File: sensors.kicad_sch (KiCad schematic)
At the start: 0 parts

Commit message: 1.2.7 Schematic design sheet #3: Sensors
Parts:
- added MK1: CMC-5042PF-AC, CMC-5042PF-AC:CUI_CMC-5042PF-AC, symbol CMC-5042PF-AC:CMC-5042PF-AC
- added Q1: TEMT6000X01, TEMT6000X01:TRANS_TEMT6000X01, symbol TEMT6000X01:TEMT6000X01
- added U2: BME280, BME280:PSON65P250X250X100-8N, symbol BME280:BME280
- added U7: MAX4466EXK, MAX4466EXK:SOT65P210X110-5N, symbol MAX4466EXK:MAX4466EXK
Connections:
- new net GND: U2.1 (GND), U2.7 (GND)

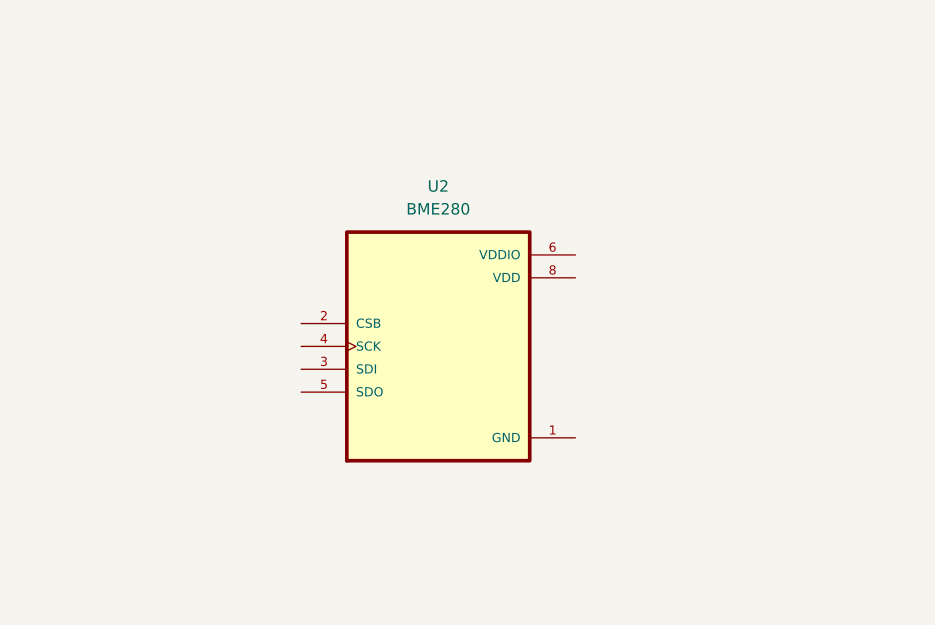
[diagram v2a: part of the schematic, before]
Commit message: 1.2.8 Design the BME280 subcircuit
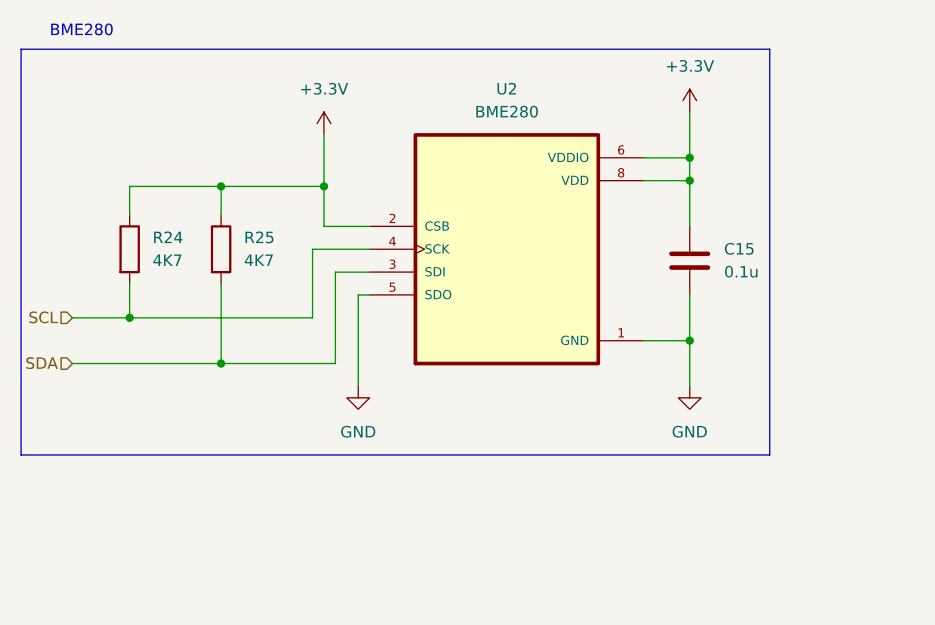
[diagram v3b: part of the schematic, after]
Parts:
- added C15: 0.1u, symbol Device:C
- added R24, R25: 4K7, symbol Device:R
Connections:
- net GND: now also U2.5 (SDO), C15.2
- net +3.3V: now reaches U2.2 (CSB)
- net +3.3V: now also U2.6 (VDDIO), U2.8 (VDD), C15.1, R24.1, R25.1
- net SDA: now reaches U2.3 (SDI)
- net SDA: now also R25.2
- net SCL: now reaches U2.4 (SCK)
- net SCL: now also R24.2
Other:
- note added: "BME280"
- moved on the sheet: U2

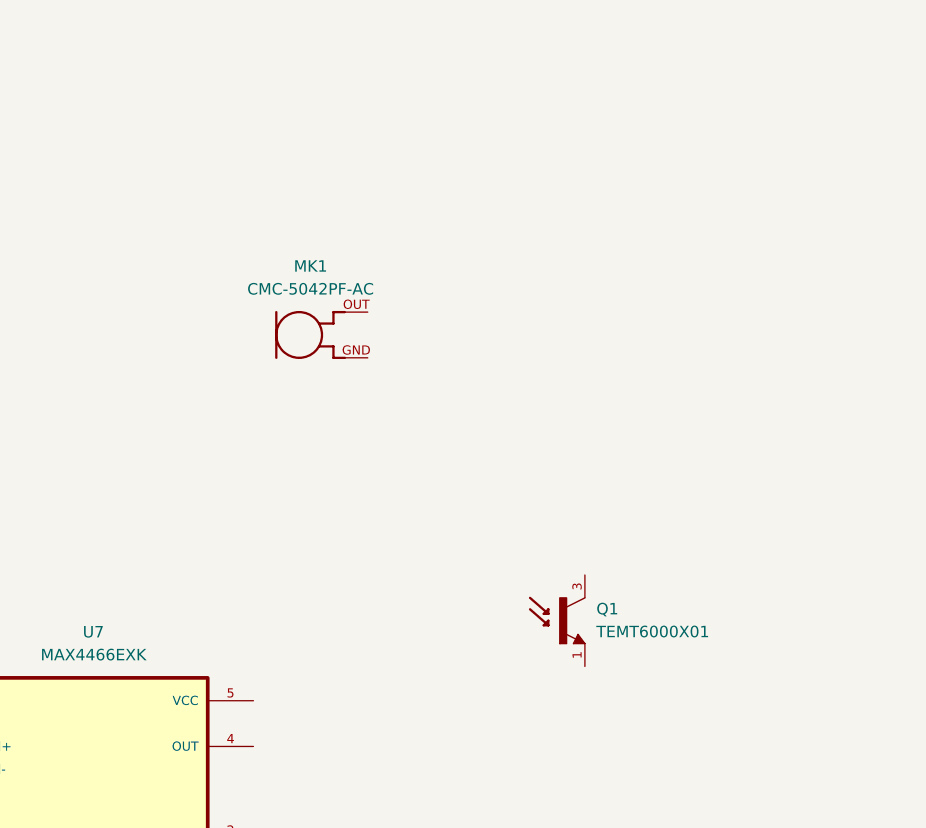
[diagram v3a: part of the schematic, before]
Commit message: 1.2.9 Design the ambient light sensor subcircuit
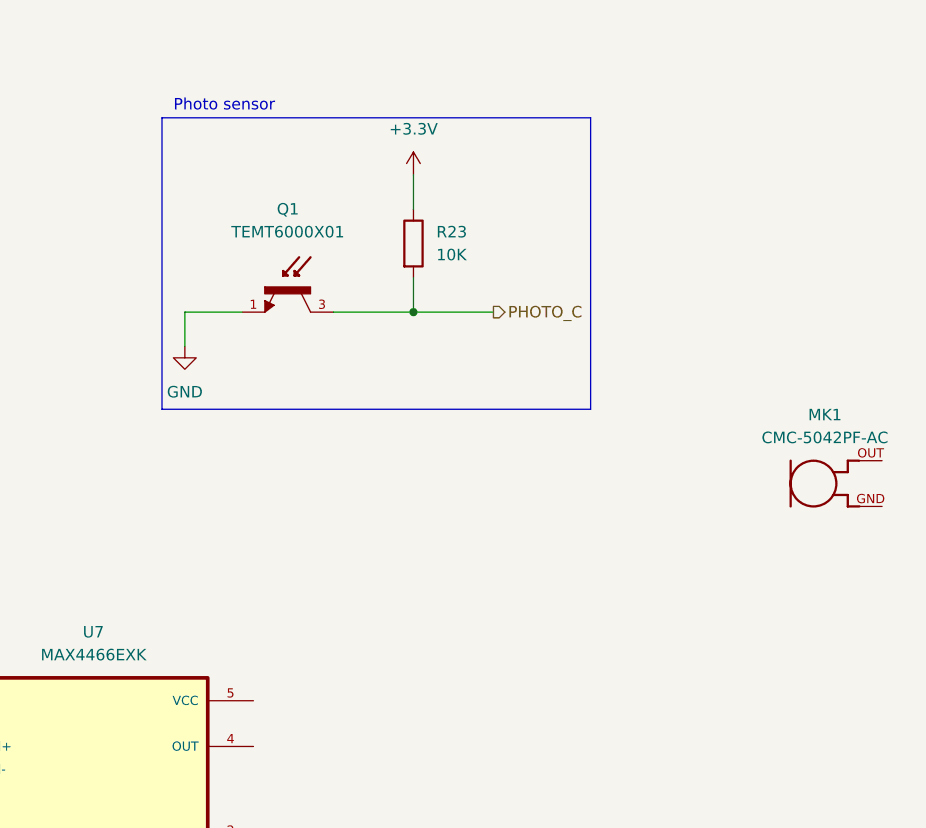
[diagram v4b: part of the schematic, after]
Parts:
- added R23: 10K, symbol Device:R
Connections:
- net +3.3V: now also R23.1
- net GND: now also Q1.1
- net PHOTO_C: now reaches Q1.3
- net PHOTO_C: now also R23.2
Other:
- note added: "Photo sensor"
- moved on the sheet: MK1, Q1

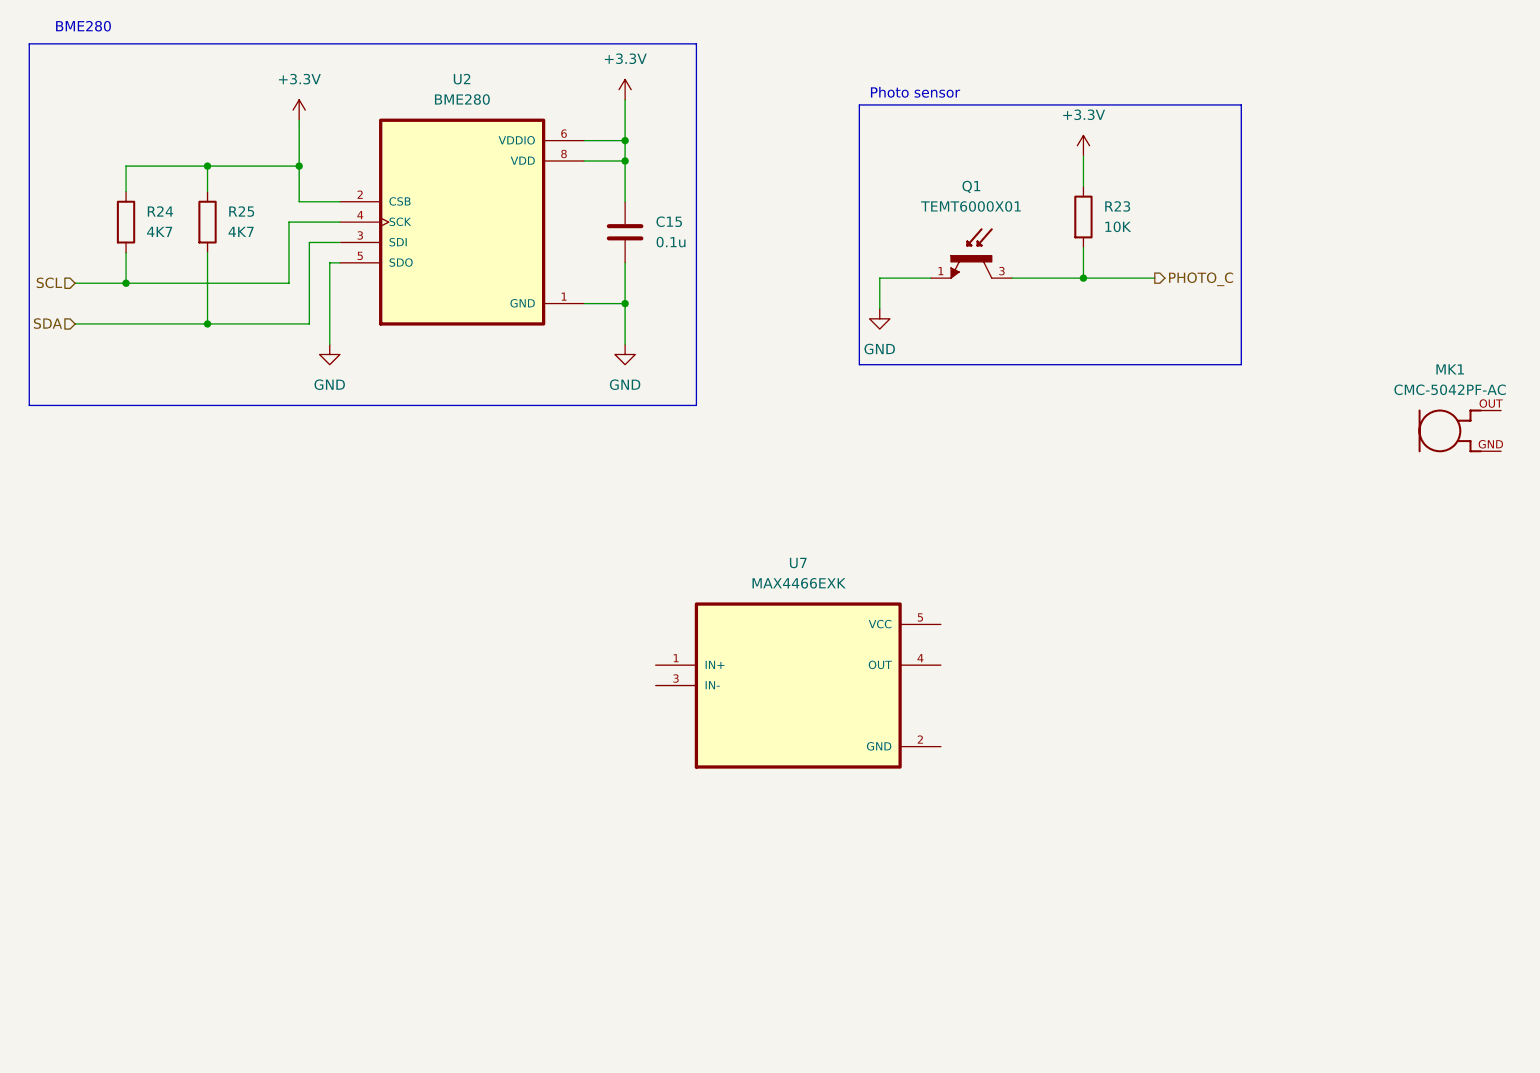
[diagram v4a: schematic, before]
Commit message: 1.3.0 Design the sound sensor subcircuit
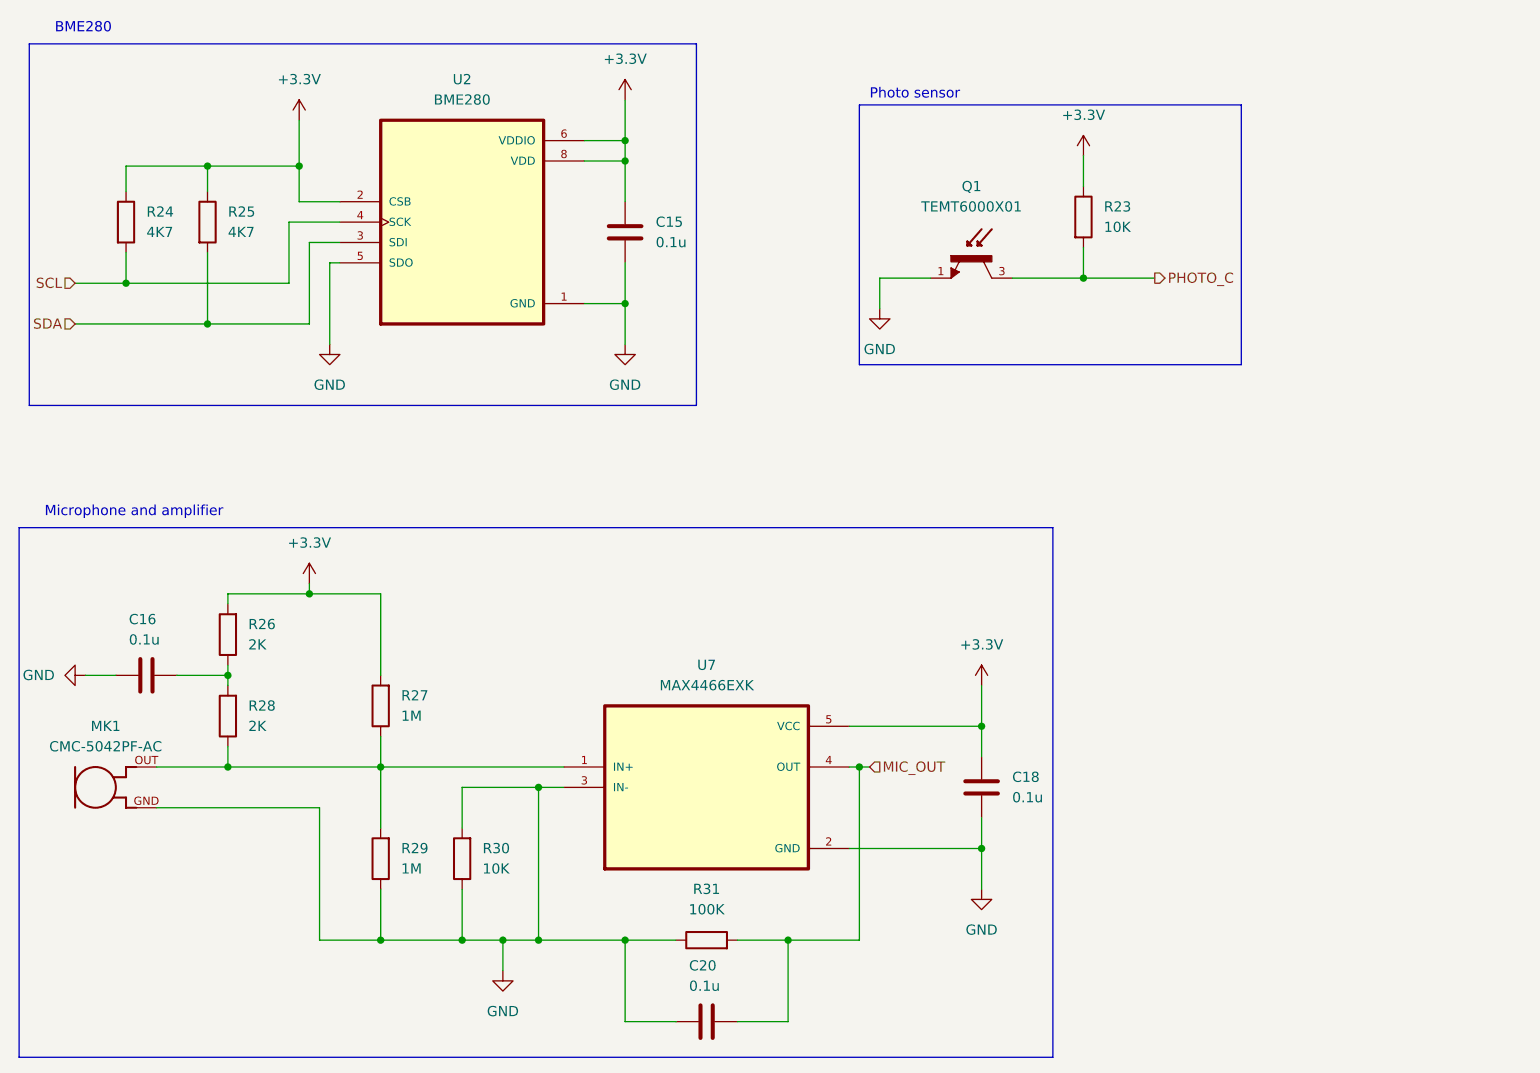
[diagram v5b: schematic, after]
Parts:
- added C16, C18, C20: 0.1u, symbol Device:C
- added R26, R28: 2K, symbol Device:R
- added R27, R29: 1M, symbol Device:R
- added R30: 10K, symbol Device:R
- added R31: 100K, symbol Device:R
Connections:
- net +3.3V: now also U7.5 (VCC), C18.1, R26.2, R27.2
- net GND: now also MK1.GND, U7.2 (GND), U7.3 (IN-), C16.1, C18.2, C20.1, R29.1, R30.1, R30.2, R31.1
- net at U7.1 (IN+): now also MK1.OUT, R27.1, R28.1, R29.2
- net MIC_OUT: now reaches U7.4 (OUT)
- net MIC_OUT: now also C20.2, R31.2
- new net: C16.2, R26.1, R28.2
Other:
- note added: "Microphone and amplifier"
- moved on the sheet: MK1, U7

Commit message: 1.3.3 Symbol and footprint associations
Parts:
- C15, C16, C18, C20: footprint (none) -> Capacitor_SMD:C_0805_2012Metric
- R23, R24, R25, R26, R27, R28, R29, R30, R31: footprint (none) -> Resistor_SMD:R_0805_2012Metric
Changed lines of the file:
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@@
 			)
 		)
-		(property "Footprint" ""
+		(property "Footprint" "Resistor_SMD:R_0805_2012Metric"
 			(at 70.358 127 90)
 			(effects
@@
 			)
 		)
-		(property "Footprint" ""
+		(property "Footprint" "Resistor_SMD:R_0805_2012Metric"
 			(at 51.308 99.06 90)
 			(effects
@@
 			)
 		)
-		(property "Footprint" ""
+		(property "Footprint" "Resistor_SMD:R_0805_2012Metric"
 			(at 35.052 47.625 90)
 			(effects
@@
 			)
 		)
-		(property "Footprint" ""
+		(property "Footprint" "Capacitor_SMD:C_0805_2012Metric"
 			(at 113.03 146.3548 0)
 			(effects
@@
 			)
 		)
-		(property "Footprint" ""
+		(property "Footprint" "Capacitor_SMD:C_0805_2012Metric"
 			(at 144.4752 121.92 0)
 			(effects
@@
 			)
 		)
-		(property "Footprint" ""
+		(property "Footprint" "Resistor_SMD:R_0805_2012Metric"
 			(at 80.518 127 90)
 			(effects
@@
 			)
 		)
-		(property "Footprint" ""
+		(property "Footprint" "Resistor_SMD:R_0805_2012Metric"
 			(at 51.308 109.22 90)
 			(effects
@@
 			)
 		)
-		(property "Footprint" ""
+		(property "Footprint" "Resistor_SMD:R_0805_2012Metric"
 			(at 109.22 138.938 90)
 			(effects
@@
 			)
 		)
-		(property "Footprint" ""
+		(property "Footprint" "Resistor_SMD:R_0805_2012Metric"
 			(at 154.432 46.99 90)
 			(effects
@@
 			)
 		)
-		(property "Footprint" ""
+		(property "Footprint" "Capacitor_SMD:C_0805_2012Metric"
 			(at 100.0252 52.705 0)
 			(effects
@@
 			)
 		)
-		(property "Footprint" ""
+		(property "Footprint" "Resistor_SMD:R_0805_2012Metric"
 			(at 70.358 107.95 90)
 			(effects
@@
 			)
 		)
-		(property "Footprint" ""
+		(property "Footprint" "Capacitor_SMD:C_0805_2012Metric"
 			(at 43.18 103.1748 0)
 			(effects
@@
 			)
 		)
-		(property "Footprint" ""
+		(property "Footprint" "Resistor_SMD:R_0805_2012Metric"
 			(at 45.212 47.625 90)
 			(effects

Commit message: 1.3.9 Bring remaining components to the layout editor
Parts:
- MK1: footprint CMC-5042PF-AC:CUI_CMC-5042PF-AC -> ESP32_demo_project:CMC-5042PF-AC
- Q1: footprint TEMT6000X01:TRANS_TEMT6000X01 -> ESP32_demo_project:TEMT6000X01
- U2: footprint BME280:PSON65P250X250X100-8N -> ESP32_demo_project:BME280
- U7: footprint MAX4466EXK:SOT65P210X110-5N -> ESP32_demo_project:MAX4466EXK
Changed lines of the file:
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@@
 			)
 		)
-		(property "Footprint" "BME280:PSON65P250X250X100-8N"
+		(property "Footprint" "ESP32_demo_project:BME280"
 			(at 78.74 47.625 0)
 			(effects
@@
 			)
 		)
-		(property "Footprint" "MAX4466EXK:SOT65P210X110-5N"
+		(property "Footprint" "ESP32_demo_project:MAX4466EXK"
 			(at 109.22 118.11 0)
 			(effects
@@
 			)
 		)
-		(property "Footprint" "CMC-5042PF-AC:CUI_CMC-5042PF-AC"
+		(property "Footprint" "ESP32_demo_project:CMC-5042PF-AC"
 			(at 33.02 118.11 0)
 			(effects
@@
 			)
 		)
-		(property "Footprint" "TEMT6000X01:TRANS_TEMT6000X01"
+		(property "Footprint" "ESP32_demo_project:TEMT6000X01"
 			(at 142.24 52.07 0)
 			(effects
